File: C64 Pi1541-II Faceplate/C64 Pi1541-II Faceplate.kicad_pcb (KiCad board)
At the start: 2 copper layers, 97.8 x 97.8 mm, 10 parts, among them IC1 0.96_OLED, J4 Faceplate, M1 Mounting, M2 Mounting, M3 Mounting, M4 Mounting

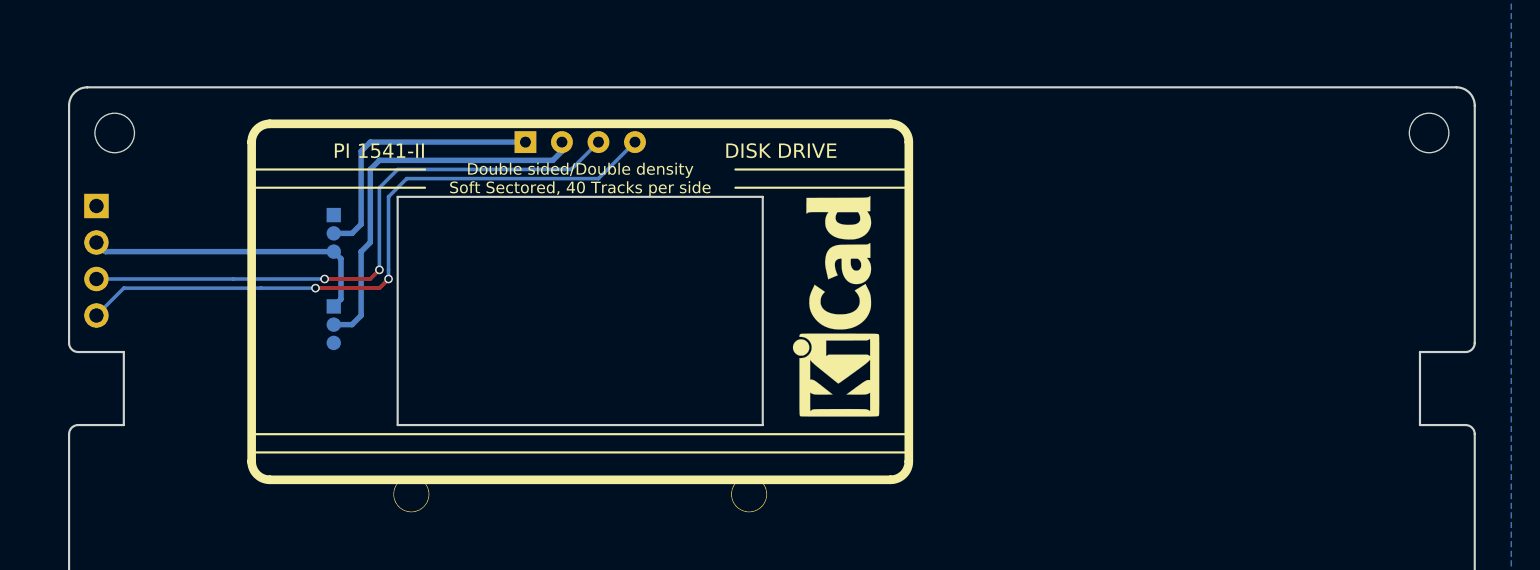
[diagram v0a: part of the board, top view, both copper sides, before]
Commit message: Added DIN cutout
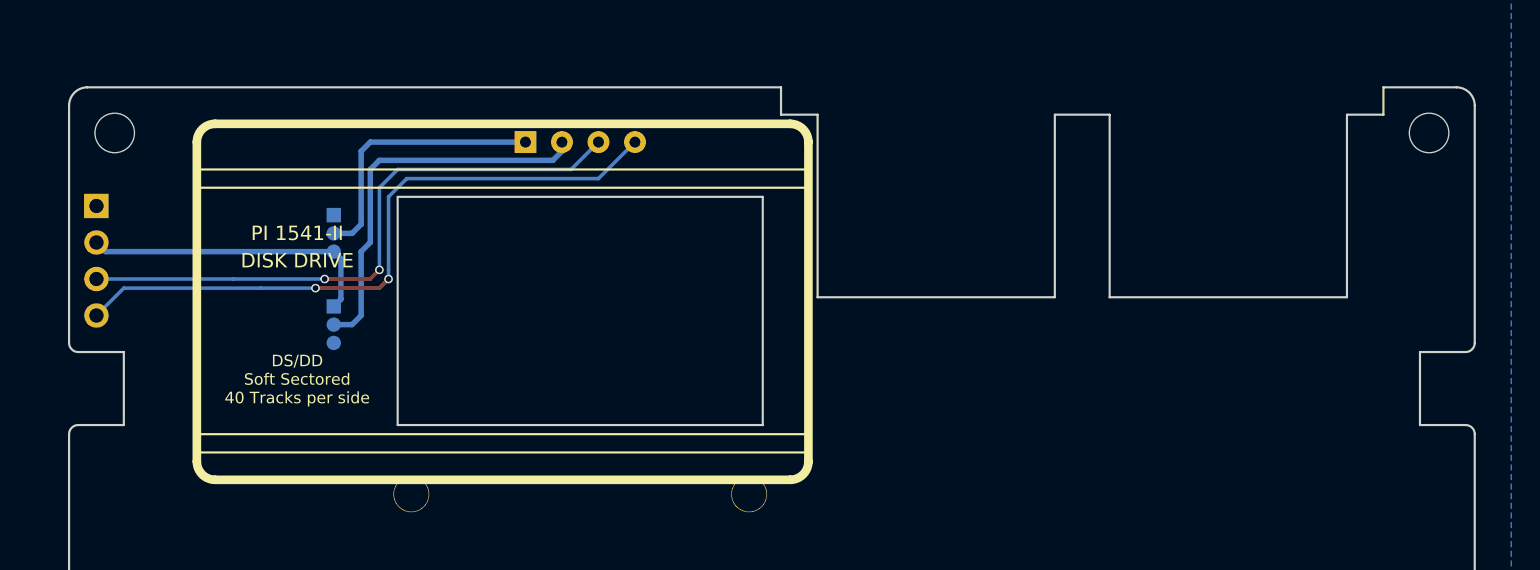
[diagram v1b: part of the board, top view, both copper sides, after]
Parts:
- removed the REF*** at (125.7, 69.8)
- moved REF*** 12.9 mm to (142.9, 88.9)
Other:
- outline, holes or cut-outs redrawn
- board text added: "DS/DD Soft Sectored 40 Tracks per side"
- board text removed: "Double sided/Double density Soft Sectored, 40 Tracks per side"

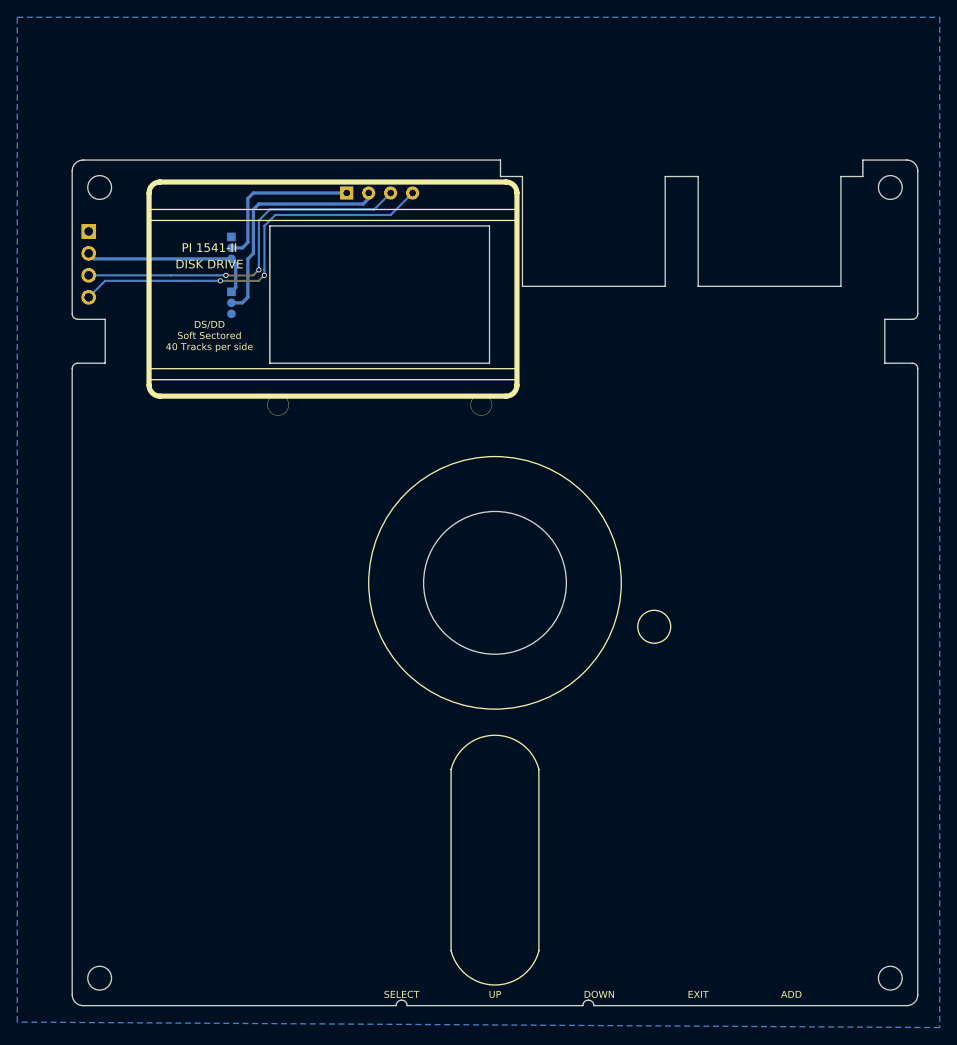
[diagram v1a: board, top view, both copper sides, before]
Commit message: Tweaked faceplate cutouts
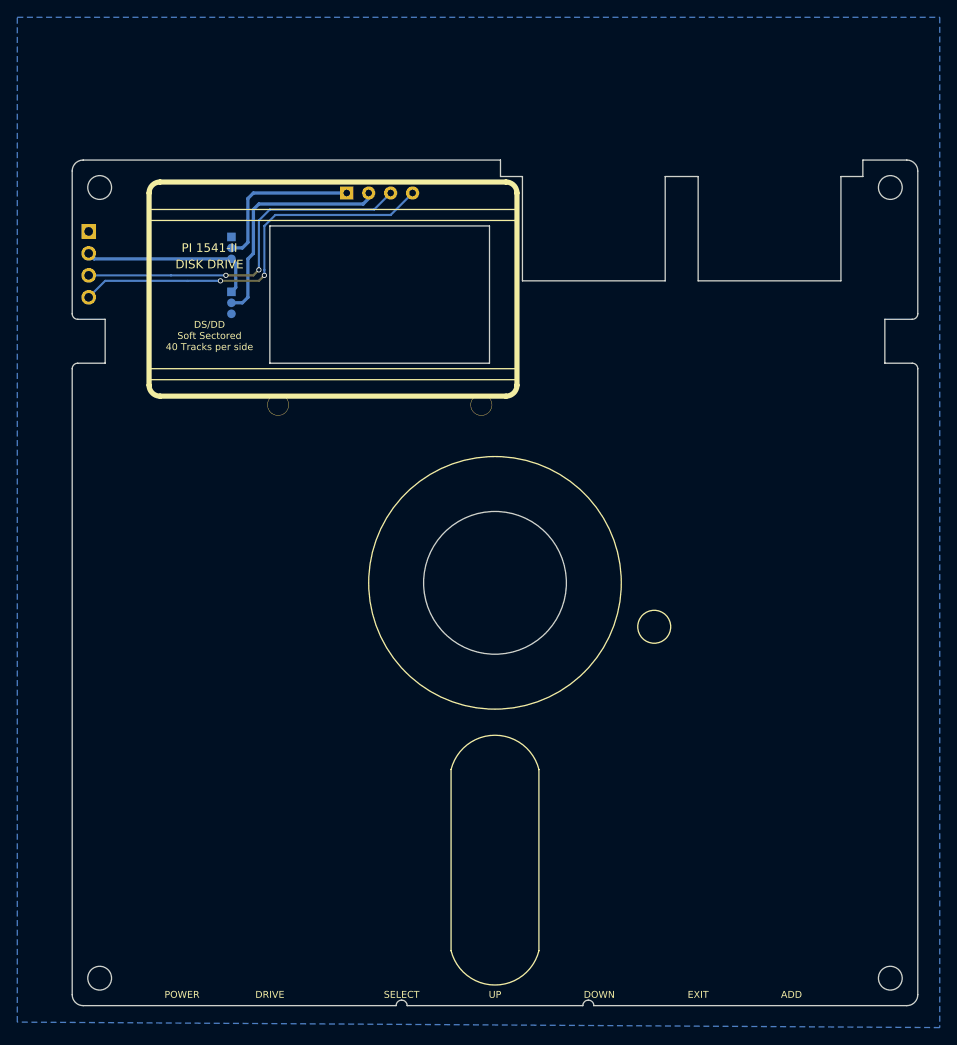
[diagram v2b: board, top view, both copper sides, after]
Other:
- outline, holes or cut-outs redrawn
- board text added: "DRIVE"
- board text added: "POWER"
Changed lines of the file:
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@@
   (general
     (thickness 1.6)
-    (drawings 89)
+    (drawings 91)
     (tracks 41)
     (zones 0)
@@
   (page A4)
   (layers
-    (0 F.Cu signal)
-    (31 B.Cu signal)
+    (0 F.Cu signal hide)
+    (31 B.Cu signal hide)
     (32 B.Adhes user)
     (33 F.Adhes user)
@@
     )
   )
+  (gr_text DRIVE (at 95.25 151.13) (layer F.SilkS)
+    (effects (font (size 0.8 0.8) (thickness 0.1)))
+  )
+  (gr_text POWER (at 85.09 151.13) (layer F.SilkS)
+    (effects (font (size 0.8 0.8) (thickness 0.1)))
+  )
   (gr_line (start 163.83 54.61) (end 168.91 54.61) (layer Edge.Cuts) (width 0.15))
   (gr_line (start 121.92 56.515) (end 124.46 56.515) (layer Edge.Cuts) (width 0.15))
@@
   (gr_line (start 163.83 56.515) (end 163.83 54.61) (layer Edge.Cuts) (width 0.15))
   (gr_line (start 161.29 56.515) (end 163.83 56.515) (layer Edge.Cuts) (width 0.15))
-  (gr_line (start 124.46 56.515) (end 124.46 69.215) (layer Edge.Cuts) (width 0.15))
-  (gr_line (start 140.97 56.515) (end 140.97 69.215) (layer Edge.Cuts) (width 0.15))
-  (gr_line (start 144.78 56.515) (end 144.78 69.215) (layer Edge.Cuts) (width 0.15))
-  (gr_line (start 161.29 56.515) (end 161.29 69.215) (layer Edge.Cuts) (width 0.15))
-  (gr_line (start 140.97 69.215) (end 124.46 69.215) (layer Edge.Cuts) (width 0.15))
-  (gr_line (start 161.29 69.215) (end 144.78 69.215) (layer Edge.Cuts) (width 0.15))
+  (gr_line (start 124.46 56.515) (end 124.46 68.58) (layer Edge.Cuts) (width 0.15))
+  (gr_line (start 140.97 56.515) (end 140.97 68.58) (layer Edge.Cuts) (width 0.15))
+  (gr_line (start 144.78 56.515) (end 144.78 68.58) (layer Edge.Cuts) (width 0.15))
+  (gr_line (start 161.29 56.515) (end 161.29 68.58) (layer Edge.Cuts) (width 0.15))
+  (gr_line (start 140.97 68.58) (end 124.46 68.58) (layer Edge.Cuts) (width 0.15))
+  (gr_line (start 161.29 68.58) (end 144.78 68.58) (layer Edge.Cuts) (width 0.15))
   (gr_text ADD (at 155.575 151.13) (layer F.SilkS)
     (effects (font (size 0.8 0.8) (thickness 0.1)))

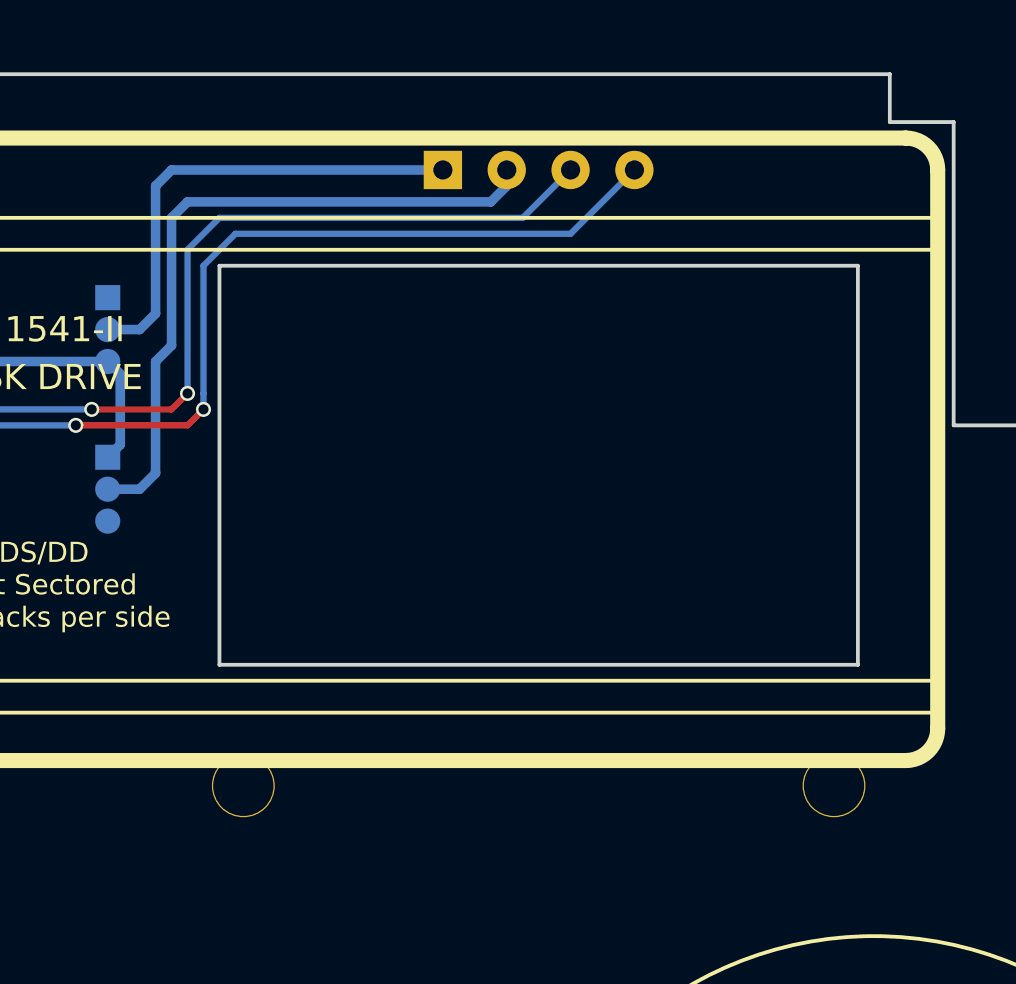
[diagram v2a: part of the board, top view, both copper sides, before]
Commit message: Moved display slightly, remove soldermask from back layer.
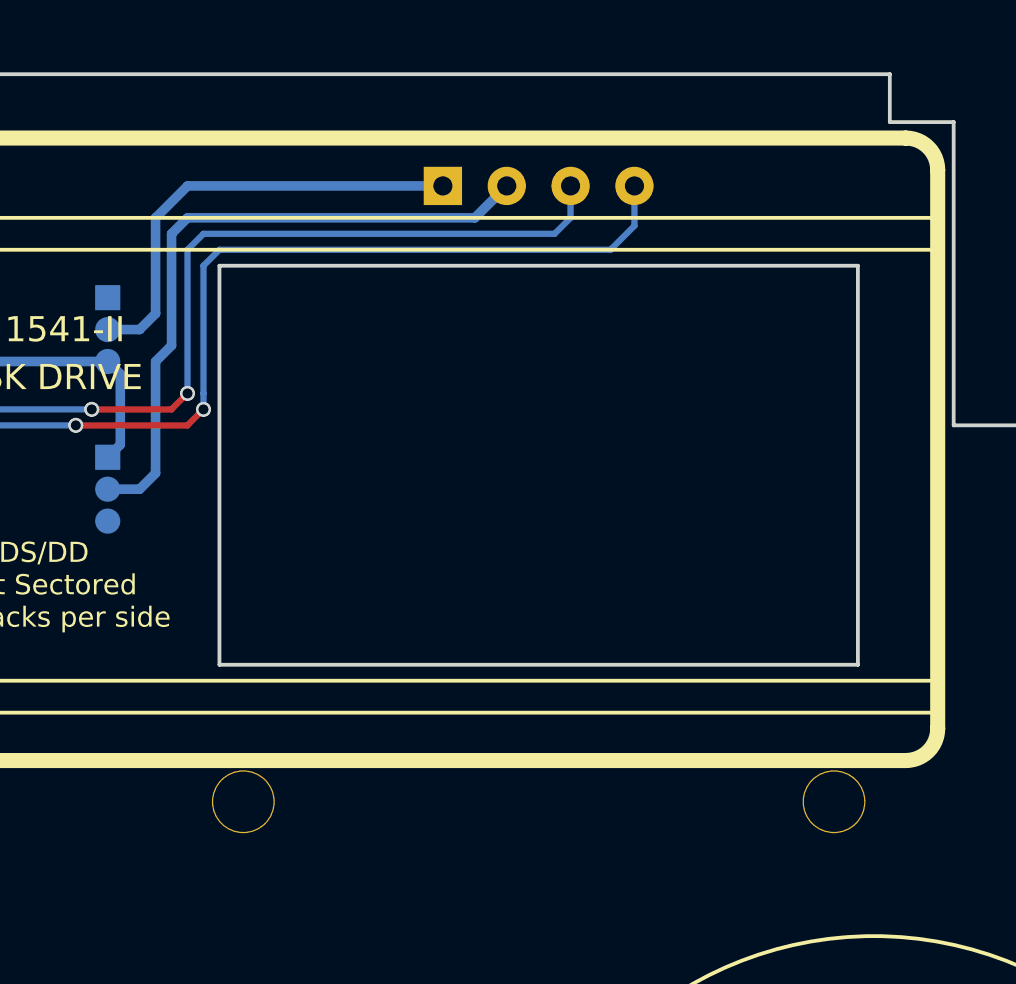
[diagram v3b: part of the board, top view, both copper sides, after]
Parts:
- moved IC1 0.63 mm to (108.0, 59.1)
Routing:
- net I2C_SCL: track 42.2 -> 43.3 mm
- net Net-(IC1-Pad2): track 27.1 -> 26.1 mm
- net Net-(IC1-Pad1): track 18.9 -> 17.9 mm
- net I2C_SDA: track 45.8 -> 46.5 mm
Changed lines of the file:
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@@
   (general
     (thickness 1.6)
-    (drawings 91)
-    (tracks 41)
+    (drawings 108)
+    (tracks 42)
     (zones 0)
     (modules 9)
@@
   )
   (module i2c_oled:0.96_I2C_OLED2 locked (layer F.Cu)
-    (at 107.95 58.42)
+    (at 107.95 59.055)
     (descr "Through hole straight pin header, 1x04, 2.54mm pitch, single row")
     (tags "Through hole pin header THT 1x04 2.54mm single row")
@@
     )
   )
+  (gr_circle (center 121.285 103.505) (end 133.985 103.505) (layer B.Mask) (width 3.8))
+  (gr_circle (center 121.285 103.505) (end 135.89 103.505) (layer B.SilkS) (width 0.15))
+  (gr_poly (pts (xy 140.335 107.95) (xy 139.065 107.95) (xy 139.065 109.22) (xy 140.335 109.22)) (layer B.Mask) (width 0.1))
+  (gr_circle (center 139.7 108.585) (end 140.335 108.585) (layer B.Mask) (width 1.15))
+  (gr_circle (center 139.7 108.585) (end 140.97 108.585) (layer B.Mask) (width 1.15))
+  (gr_circle (center 139.7 108.585) (end 141.605 108.585) (layer B.SilkS) (width 0.15))
+  (gr_arc (start 121.285 127) (end 116.84 125.73) (angle 142.2531762) (layer B.Mask) (width 1.25))
+  (gr_arc (start 121.285 127.635) (end 116.84 126.365) (angle 142.2531923) (layer B.Mask) (width 1.25))
+  (gr_arc (start 121.285 126.365) (end 116.84 125.095) (angle 148.1092082) (layer B.Mask) (width 1.25))
+  (gr_arc (start 121.285 127) (end 118.11 125.73) (angle 136.397181) (layer B.Mask) (width 1.25))
+  (gr_poly (pts (xy 126.365 125.095) (xy 116.205 125.095) (xy 116.205 146.05) (xy 126.365 146.05)) (layer B.Mask) (width 0.1))
+  (gr_arc (start 121.285 144.78) (end 125.73 146.05) (angle 148.1092082) (layer B.Mask) (width 1.25))
+  (gr_arc (start 121.285 142.875) (end 124.46 144.145) (angle 136.397181) (layer B.Mask) (width 1.25))
+  (gr_arc (start 121.285 143.51) (end 124.46 144.78) (angle 136.397181) (layer B.Mask) (width 1.25))
+  (gr_arc (start 121.285 128.27) (end 118.11 127) (angle 136.397181) (layer B.Mask) (width 1.25))
+  (gr_arc (start 121.285 143.51) (end 125.73 144.78) (angle 142.2531923) (layer B.Mask) (width 1.25))
+  (gr_arc (start 121.285 144.145) (end 125.73 145.415) (angle 148.1092082) (layer B.Mask) (width 1.25))
   (gr_text DRIVE (at 95.25 151.13) (layer F.SilkS)
     (effects (font (size 0.8 0.8) (thickness 0.1)))
@@
   (segment (start 74.93 66.04) (end 74.295 65.405) (width 0.381) (layer B.Cu) (net 2))
   (segment (start 90.805 66.04) (end 74.93 66.04) (width 0.381) (layer B.Cu) (net 2))
-  (segment (start 106.045 59.69) (end 106.68 59.055) (width 0.381) (layer B.Cu) (net 3))
-  (segment (start 93.98 59.69) (end 106.045 59.69) (width 0.381) (layer B.Cu) (net 3))
-  (segment (start 93.345 60.325) (end 93.98 59.69) (width 0.381) (layer B.Cu) (net 3))
+  (segment (start 93.345 60.96) (end 93.98 60.325) (width 0.381) (layer B.Cu) (net 3))
   (segment (start 92.075 71.12) (end 92.71 70.485) (width 0.381) (layer B.Cu) (net 3))
+  (segment (start 92.71 66.04) (end 93.345 65.405) (width 0.381) (layer B.Cu) (net 3))
+  (segment (start 105.41 60.325) (end 106.68 59.055) (width 0.381) (layer B.Cu) (net 3))
+  (segment (start 93.98 60.325) (end 105.41 60.325) (width 0.381) (layer B.Cu) (net 3))
   (segment (start 90.805 71.12) (end 92.075 71.12) (width 0.381) (layer B.Cu) (net 3))
-  (segment (start 106.68 59.055) (end 106.68 58.42) (width 0.381) (layer B.Cu) (net 3))
+  (segment (start 93.345 65.405) (end 93.345 60.96) (width 0.381) (layer B.Cu) (net 3))
   (segment (start 92.71 70.485) (end 92.71 66.04) (width 0.381) (layer B.Cu) (net 3))
-  (segment (start 92.71 66.04) (end 93.345 65.405) (width 0.381) (layer B.Cu) (net 3))
-  (segment (start 93.345 65.405) (end 93.345 60.325) (width 0.381) (layer B.Cu) (net 3))
   (via (at 90.17 67.945) (size 0.6) (drill 0.4) (layers F.Cu B.Cu) (net 4))
   (via (at 93.98 67.31) (size 0.6) (drill 0.4) (layers F.Cu B.Cu) (net 4))
   (segment (start 90.17 67.945) (end 93.345 67.945) (width 0.25) (layer F.Cu) (net 4))
   (segment (start 93.345 67.945) (end 93.98 67.31) (width 0.25) (layer F.Cu) (net 4))
-  (segment (start 93.98 61.595) (end 93.98 67.31) (width 0.25) (layer B.Cu) (net 4))
-  (segment (start 109.22 58.42) (end 107.315 60.325) (width 0.25) (layer B.Cu) (net 4))
-  (segment (start 95.25 60.325) (end 93.98 61.595) (width 0.25) (layer B.Cu) (net 4))
-  (segment (start 107.315 60.325) (end 95.25 60.325) (width 0.25) (layer B.Cu) (net 4))
   (segment (start 83.82 67.945) (end 74.295 67.945) (width 0.25) (layer B.Cu) (net 4))
   (segment (start 90.17 67.945) (end 83.82 67.945) (width 0.25) (layer B.Cu) (net 4))
+  (segment (start 94.615 60.96) (end 93.98 61.595) (width 0.25) (layer B.Cu) (net 4))
+  (segment (start 108.585 60.96) (end 94.615 60.96) (width 0.25) (layer B.Cu) (net 4))
+  (segment (start 93.98 61.595) (end 93.98 67.31) (width 0.25) (layer B.Cu) (net 4))
+  (segment (start 109.22 58.42) (end 109.22 60.325) (width 0.25) (layer B.Cu) (net 4))
+  (segment (start 109.22 60.325) (end 108.585 60.96) (width 0.25) (layer B.Cu) (net 4))
   (via (at 89.535 68.58) (size 0.6) (drill 0.4) (layers F.Cu B.Cu) (net 5))
   (segment (start 89.535 68.58) (end 85.725 68.58) (width 0.25) (layer B.Cu) (net 5))
@@
   (via (at 94.615 67.945) (size 0.6) (drill 0.4) (layers F.Cu B.Cu) (net 5))
   (segment (start 93.98 68.58) (end 94.615 67.945) (width 0.25) (layer F.Cu) (net 5))
-  (segment (start 94.615 67.31) (end 94.615 67.945) (width 0.25) (layer B.Cu) (net 5))
-  (segment (start 94.615 62.23) (end 94.615 67.31) (width 0.25) (layer B.Cu) (net 5))
-  (segment (start 95.885 60.96) (end 94.615 62.23) (width 0.25) (layer B.Cu) (net 5))
-  (segment (start 111.76 58.42) (end 109.22 60.96) (width 0.25) (layer B.Cu) (net 5))
-  (segment (start 109.22 60.96) (end 95.885 60.96) (width 0.25) (layer B.Cu) (net 5))
   (segment (start 76.2 68.58) (end 74.295 70.485) (width 0.25) (layer B.Cu) (net 5))
   (segment (start 85.725 68.58) (end 76.2 68.58) (width 0.25) (layer B.Cu) (net 5))
-  (segment (start 93.345 58.42) (end 104.14 58.42) (width 0.381) (layer B.Cu) (net 6))
-  (segment (start 92.71 59.055) (end 93.345 58.42) (width 0.381) (layer B.Cu) (net 6))
+  (segment (start 94.615 67.31) (end 94.615 67.945) (width 0.25) (layer B.Cu) (net 5))
+  (segment (start 111.76 60.6425) (end 110.8075 61.595) (width 0.25) (layer B.Cu) (net 5))
+  (segment (start 111.76 59.055) (end 111.76 60.6425) (width 0.25) (layer B.Cu) (net 5))
+  (segment (start 95.25 61.595) (end 94.615 62.23) (width 0.25) (layer B.Cu) (net 5))
+  (segment (start 110.8075 61.595) (end 95.25 61.595) (width 0.25) (layer B.Cu) (net 5))
+  (segment (start 94.615 62.23) (end 94.615 67.31) (width 0.25) (layer B.Cu) (net 5))
+  (segment (start 92.71 64.135) (end 92.71 60.325) (width 0.381) (layer B.Cu) (net 6))
+  (segment (start 93.98 59.055) (end 104.14 59.055) (width 0.381) (layer B.Cu) (net 6))
+  (segment (start 92.71 60.325) (end 93.98 59.055) (width 0.381) (layer B.Cu) (net 6))
   (segment (start 90.805 64.77) (end 92.075 64.77) (width 0.381) (layer B.Cu) (net 6))
-  (segment (start 92.71 64.135) (end 92.71 59.055) (width 0.381) (layer B.Cu) (net 6))
   (segment (start 92.075 64.77) (end 92.71 64.135) (width 0.381) (layer B.Cu) (net 6))
   (zone (net 1) (net_name GND) (layer B.Cu) (hatch edge 0.508)
